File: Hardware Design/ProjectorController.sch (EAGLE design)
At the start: 12 parts, among them J1 5747844-4, J2 Cap Buttons, J3 Prog, J4 Prog/Run, U1 ESP-WROOM-32, U2 SP3232EEN-L

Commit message: USB port added and rough cut of schematic done. PC-11
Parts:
- added J5: 10118194-0001LF, 10118194-0001LF:10118194-0001LF
- R2: value (none) -> 10K
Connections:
- new net 3V3: C1.1, J3.4, J4.3, R1.1, U$1.OUT, U1.3V3, U2.VCC
- new net 5V: C2.1, J5.1, U$1.IN
- new net N$10: J1.2, U2.T1OUT
- new net N$11: J1.3, U2.R1OUT
- new net N$12: U1.IO14, U2.T1IN
- new net N$13: U1.IO12, U2.R1IN
- new net N$3: J2.3, U1.IO4
- new net N$4: R1.2, S1.2, U1.EN
- new net N$5: R2.2, U1.IO0
- new net N$6: J4.2, R2.1
- new net N$7: J3.3, U1.TXD0
- new net N$8: J3.2, U1.RXD0
- net GND: now also J1.5, J3.1, J4.1, J5.5, S1.1
- net N$1: now also J2.1, U1.IO15; no longer C1.1, U$1.OUT, U1.3V3
- net N$2: now also J2.2, U1.IO33; no longer C2.1, U$1.IN
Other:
- moved on the sheet: C1, C2, J3, J4, R1, R2, S1, U$1

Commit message: Progress on board layout PC-13
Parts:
- added C3, C4, C5, C6, C7: 0.1uF, SparkFun-Capacitors:CAP-1206
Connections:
- new net N$12: C5.2, U2.C1+
- new net N$14: C5.1, U2.C1-
- new net N$15: C4.2, U2.C2+
- new net N$16: C4.1, U2.C2-
- new net N$17: C7.2, U2.V+
- new net N$19: C6.2, U2.V-
- net 3V3: now also C3.2
- net GND: now also C3.1, C6.1, C7.1
- net N$7: now also J3.2; no longer J3.3
- net N$8: now also J3.3; no longer J3.2
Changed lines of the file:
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@@
 <part name="C2" library="SparkFun-Capacitors" deviceset="CAP" device="-1206"/>
 <part name="J5" library="10118194-0001LF" deviceset="10118194-0001LF" device=""/>
+<part name="C3" library="SparkFun-Capacitors" deviceset="CAP" device="-1206" value="0.1uF"/>
+<part name="C4" library="SparkFun-Capacitors" deviceset="CAP" device="-1206" value="0.1uF"/>
+<part name="C5" library="SparkFun-Capacitors" deviceset="CAP" device="-1206" value="0.1uF"/>
+<part name="C6" library="SparkFun-Capacitors" deviceset="CAP" device="-1206" value="0.1uF"/>
+<part name="C7" library="SparkFun-Capacitors" deviceset="CAP" device="-1206" value="0.1uF"/>
 </parts>
 <sheets>
@@
 <attribute name="NAME" x="-94.224959375" y="24.8851" size="1.271559375" layer="95" rot="R180"/>
 <attribute name="VALUE" x="-93.976059375" y="48.2639" size="1.270659375" layer="96" rot="R180"/>
+</instance>
+<instance part="C3" gate="G$1" x="40.64" y="45.72" smashed="yes">
+<attribute name="NAME" x="42.164" y="48.641" size="1.778" layer="95" font="vector"/>
+<attribute name="VALUE" x="42.164" y="43.561" size="1.778" layer="96" font="vector"/>
+</instance>
+<instance part="C4" gate="G$1" x="33.02" y="30.48" smashed="yes" rot="R180">
+<attribute name="NAME" x="31.496" y="27.559" size="1.778" layer="95" font="vector" rot="R180"/>
+<attribute name="VALUE" x="31.496" y="32.639" size="1.778" layer="96" font="vector" rot="R180"/>
+</instance>
+<instance part="C5" gate="G$1" x="38.1" y="35.56" smashed="yes" rot="R180">
+<attribute name="NAME" x="36.576" y="32.639" size="1.778" layer="95" font="vector" rot="R180"/>
+<attribute name="VALUE" x="36.576" y="37.719" size="1.778" layer="96" font="vector" rot="R180"/>
+</instance>
+<instance part="C6" gate="G$1" x="38.1" y="12.7" smashed="yes" rot="R90">
+<attribute name="NAME" x="35.179" y="14.224" size="1.778" layer="95" font="vector" rot="R90"/>
+<attribute name="VALUE" x="40.259" y="14.224" size="1.778" layer="96" font="vector" rot="R90"/>
+</instance>
+<instance part="C7" gate="G$1" x="33.02" y="40.64" smashed="yes" rot="R90">
+<attribute name="NAME" x="30.099" y="42.164" size="1.778" layer="95" font="vector" rot="R90"/>
+<attribute name="VALUE" x="35.179" y="42.164" size="1.778" layer="96" font="vector" rot="R90"/>
 </instance>
 </instances>
@@
 <wire x1="43.18" y1="7.62" x2="38.1" y2="7.62" width="0.1524" layer="91"/>
 <label x="33.02" y="7.62" size="1.778" layer="95"/>
+<pinref part="C6" gate="G$1" pin="1"/>
+<wire x1="33.02" y1="12.7" x2="33.02" y2="10.16" width="0.1524" layer="91"/>
+<wire x1="33.02" y1="10.16" x2="38.1" y2="10.16" width="0.1524" layer="91"/>
+<wire x1="38.1" y1="10.16" x2="38.1" y2="7.62" width="0.1524" layer="91"/>
 </segment>
 <segment>
@@
 <wire x1="99.06" y1="15.24" x2="93.98" y2="15.24" width="0.1524" layer="91"/>
 <label x="91.44" y="15.24" size="1.778" layer="95"/>
+</segment>
+<segment>
+<pinref part="C3" gate="G$1" pin="1"/>
+<wire x1="40.64" y1="50.8" x2="40.64" y2="53.34" width="0.1524" layer="91"/>
+<label x="40.64" y="53.34" size="1.778" layer="95"/>
+</segment>
+<segment>
+<pinref part="C7" gate="G$1" pin="1"/>
+<wire x1="27.94" y1="40.64" x2="25.4" y2="40.64" width="0.1524" layer="91"/>
+<label x="22.86" y="40.64" size="1.778" layer="95"/>
 </segment>
 </net>
@@
 <segment>
 <pinref part="U2" gate="A" pin="VCC"/>
-<wire x1="43.18" y1="43.18" x2="38.1" y2="43.18" width="0.1524" layer="91"/>
+<wire x1="43.18" y1="43.18" x2="40.64" y2="43.18" width="0.1524" layer="91"/>
 <label x="35.56" y="43.18" size="1.778" layer="95"/>
+<pinref part="C3" gate="G$1" pin="2"/>
+<wire x1="40.64" y1="43.18" x2="38.1" y2="43.18" width="0.1524" layer="91"/>
+<junction x="40.64" y="43.18"/>
 </segment>
 </net>
@@
 <pinref part="U1" gate="G$1" pin="TXD0"/>
 <wire x1="-30.48" y1="38.1" x2="-45.72" y2="38.1" width="0.1524" layer="91"/>
-<wire x1="-45.72" y1="38.1" x2="-45.72" y2="30.48" width="0.1524" layer="91"/>
-<pinref part="J3" gate="J1" pin="3"/>
-<wire x1="-45.72" y1="30.48" x2="-66.04" y2="30.48" width="0.1524" layer="91"/>
+<wire x1="-45.72" y1="38.1" x2="-45.72" y2="27.94" width="0.1524" layer="91"/>
+<pinref part="J3" gate="J1" pin="2"/>
+<wire x1="-66.04" y1="27.94" x2="-45.72" y2="27.94" width="0.1524" layer="91"/>
 </segment>
 </net>
@@
 <pinref part="U1" gate="G$1" pin="RXD0"/>
 <wire x1="-30.48" y1="35.56" x2="-43.18" y2="35.56" width="0.1524" layer="91"/>
-<wire x1="-43.18" y1="35.56" x2="-43.18" y2="27.94" width="0.1524" layer="91"/>
-<pinref part="J3" gate="J1" pin="2"/>
-<wire x1="-43.18" y1="27.94" x2="-66.04" y2="27.94" width="0.1524" layer="91"/>
+<wire x1="-43.18" y1="35.56" x2="-43.18" y2="30.48" width="0.1524" layer="91"/>
+<pinref part="J3" gate="J1" pin="3"/>
+<wire x1="-66.04" y1="30.48" x2="-43.18" y2="30.48" width="0.1524" layer="91"/>
 </segment>
 </net>
@@
 <pinref part="J1" gate="G$1" pin="3"/>
 <wire x1="88.9" y1="25.4" x2="99.06" y2="25.4" width="0.1524" layer="91"/>
-</segment>
-</net>
-<net name="N$12" class="0">
-<segment>
-<pinref part="U1" gate="G$1" pin="IO14"/>
-<wire x1="10.16" y1="43.18" x2="30.48" y2="43.18" width="0.1524" layer="91"/>
-<wire x1="30.48" y1="43.18" x2="30.48" y2="17.78" width="0.1524" layer="91"/>
-<pinref part="U2" gate="A" pin="T1IN"/>
-<wire x1="30.48" y1="17.78" x2="43.18" y2="17.78" width="0.1524" layer="91"/>
 </segment>
 </net>
@@
 </segment>
 </net>
+<net name="N$9" class="0">
+<segment>
+<pinref part="U2" gate="A" pin="T1IN"/>
+<wire x1="22.86" y1="17.78" x2="43.18" y2="17.78" width="0.1524" layer="91"/>
+<pinref part="U1" gate="G$1" pin="IO14"/>
+<wire x1="10.16" y1="43.18" x2="22.86" y2="43.18" width="0.1524" layer="91"/>
+<wire x1="22.86" y1="17.78" x2="22.86" y2="43.18" width="0.1524" layer="91"/>
+</segment>
+</net>
+<net name="N$12" class="0">
+<segment>
+<pinref part="C5" gate="G$1" pin="2"/>
+<pinref part="U2" gate="A" pin="C1+"/>
+<wire x1="38.1" y1="38.1" x2="43.18" y2="38.1" width="0.1524" layer="91"/>
+<wire x1="43.18" y1="38.1" x2="43.18" y2="35.56" width="0.1524" layer="91"/>
+</segment>
+</net>
+<net name="N$14" class="0">
+<segment>
+<pinref part="U2" gate="A" pin="C1-"/>
+<wire x1="43.18" y1="33.02" x2="40.64" y2="33.02" width="0.1524" layer="91"/>
+<wire x1="40.64" y1="33.02" x2="40.64" y2="30.48" width="0.1524" layer="91"/>
+<pinref part="C5" gate="G$1" pin="1"/>
+<wire x1="40.64" y1="30.48" x2="38.1" y2="30.48" width="0.1524" layer="91"/>
+</segment>
+</net>
+<net name="N$15" class="0">
+<segment>
+<pinref part="U2" gate="A" pin="C2+"/>
+<wire x1="43.18" y1="30.48" x2="41.656" y2="30.48" width="0.1524" layer="91"/>
+<wire x1="41.656" y1="30.48" x2="41.656" y2="28.956" width="0.1524" layer="91"/>
+<wire x1="41.656" y1="28.956" x2="41.91" y2="28.956" width="0.1524" layer="91"/>
+<wire x1="41.656" y1="28.956" x2="35.56" y2="28.956" width="0.1524" layer="91"/>
+<wire x1="35.56" y1="28.956" x2="35.56" y2="33.02" width="0.1524" layer="91"/>
+<pinref part="C4" gate="G$1" pin="2"/>
+<wire x1="35.56" y1="33.02" x2="33.02" y2="33.02" width="0.1524" layer="91"/>
+</segment>
+</net>
+<net name="N$16" class="0">
+<segment>
+<pinref part="U2" gate="A" pin="C2-"/>
+<wire x1="43.18" y1="27.94" x2="35.56" y2="27.94" width="0.1524" layer="91"/>
+<wire x1="35.56" y1="27.94" x2="35.56" y2="25.4" width="0.1524" layer="91"/>
+<pinref part="C4" gate="G$1" pin="1"/>
+<wire x1="35.56" y1="25.4" x2="33.02" y2="25.4" width="0.1524" layer="91"/>
+</segment>
+</net>
+<net name="N$17" class="0">
+<segment>
+<pinref part="U2" gate="A" pin="V+"/>
+<pinref part="C7" gate="G$1" pin="2"/>
+<wire x1="43.18" y1="40.64" x2="35.56" y2="40.64" width="0.1524" layer="91"/>
+</segment>
+</net>
+<net name="N$19" class="0">
+<segment>
+<pinref part="U2" gate="A" pin="V-"/>
+<pinref part="C6" gate="G$1" pin="2"/>
+<wire x1="43.18" y1="10.16" x2="40.64" y2="10.16" width="0.1524" layer="91"/>
+<wire x1="40.64" y1="10.16" x2="40.64" y2="12.7" width="0.1524" layer="91"/>
+</segment>
+</net>

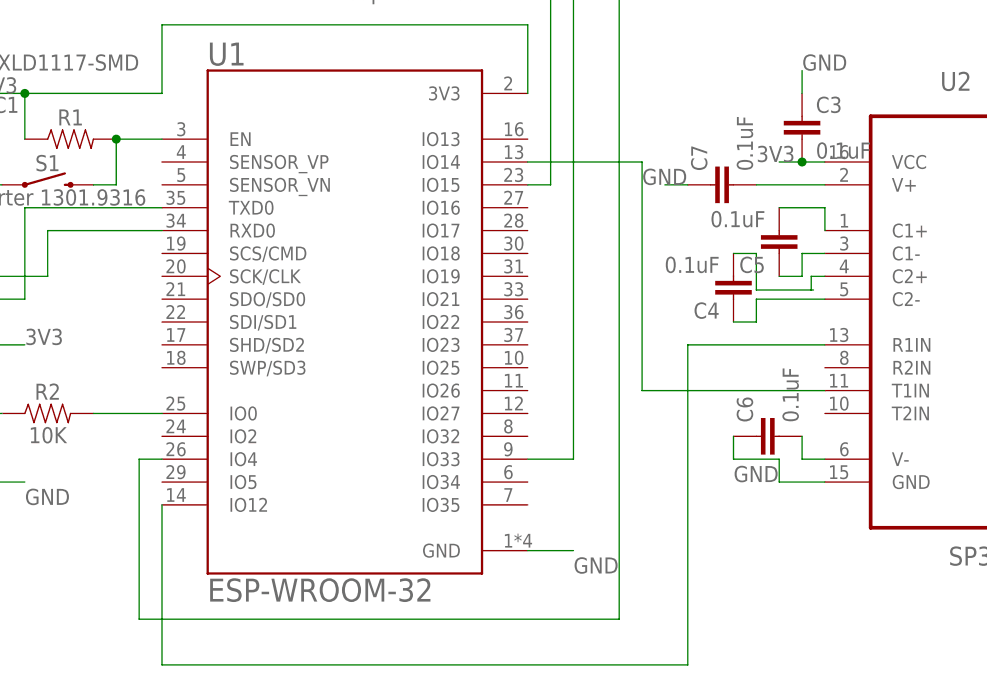
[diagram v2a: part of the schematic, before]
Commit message: Switched UART Pins PC-12
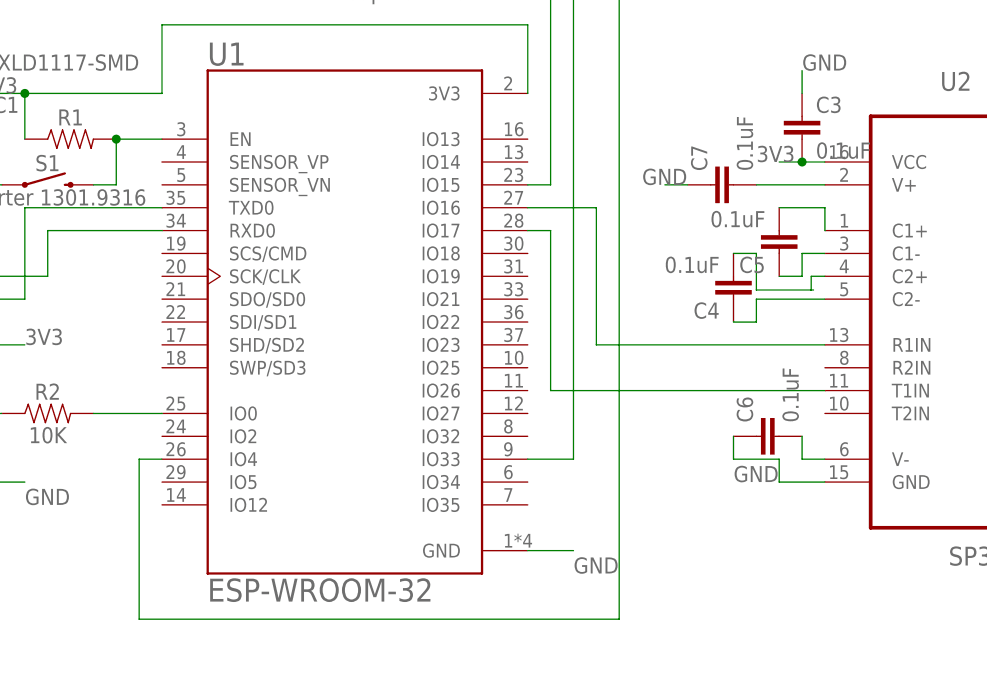
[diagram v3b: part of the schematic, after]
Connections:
- net N$13: now also U1.IO16; no longer U1.IO12
- net N$9: now also U1.IO17; no longer U1.IO14
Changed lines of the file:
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@@
 <net name="N$13" class="0">
 <segment>
-<pinref part="U1" gate="G$1" pin="IO12"/>
-<wire x1="-30.48" y1="5.08" x2="-30.48" y2="-12.7" width="0.1524" layer="91"/>
-<wire x1="-30.48" y1="-12.7" x2="27.94" y2="-12.7" width="0.1524" layer="91"/>
-<wire x1="27.94" y1="-12.7" x2="27.94" y2="22.86" width="0.1524" layer="91"/>
 <pinref part="U2" gate="A" pin="R1IN"/>
-<wire x1="27.94" y1="22.86" x2="43.18" y2="22.86" width="0.1524" layer="91"/>
+<wire x1="17.78" y1="22.86" x2="43.18" y2="22.86" width="0.1524" layer="91"/>
+<pinref part="U1" gate="G$1" pin="IO16"/>
+<wire x1="10.16" y1="38.1" x2="17.78" y2="38.1" width="0.1524" layer="91"/>
+<wire x1="17.78" y1="38.1" x2="17.78" y2="22.86" width="0.1524" layer="91"/>
 </segment>
 </net>
@@
 <segment>
 <pinref part="U2" gate="A" pin="T1IN"/>
-<wire x1="22.86" y1="17.78" x2="43.18" y2="17.78" width="0.1524" layer="91"/>
-<pinref part="U1" gate="G$1" pin="IO14"/>
-<wire x1="10.16" y1="43.18" x2="22.86" y2="43.18" width="0.1524" layer="91"/>
-<wire x1="22.86" y1="17.78" x2="22.86" y2="43.18" width="0.1524" layer="91"/>
+<wire x1="12.7" y1="17.78" x2="43.18" y2="17.78" width="0.1524" layer="91"/>
+<pinref part="U1" gate="G$1" pin="IO17"/>
+<wire x1="10.16" y1="35.56" x2="12.7" y2="35.56" width="0.1524" layer="91"/>
+<wire x1="12.7" y1="35.56" x2="12.7" y2="17.78" width="0.1524" layer="91"/>
 </segment>
 </net>

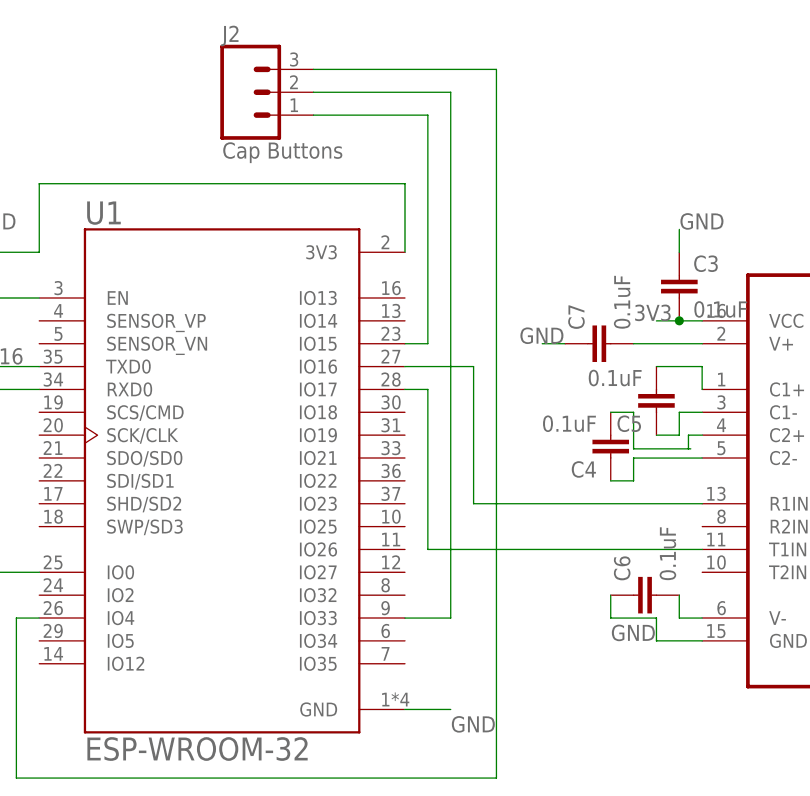
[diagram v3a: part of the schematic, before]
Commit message: Board Layout Complete PC-13
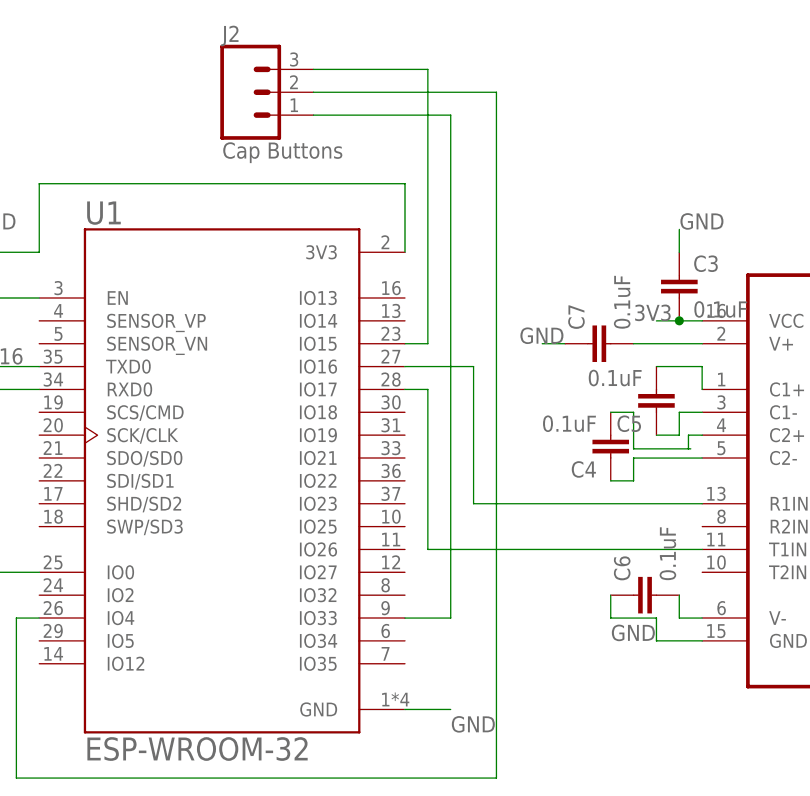
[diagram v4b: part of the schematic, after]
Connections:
- net N$1: now also J2.3; no longer J2.1
- net N$2: now also J2.1; no longer J2.2
- net N$3: now also J2.2; no longer J2.3
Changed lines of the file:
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@@
 <pinref part="U1" gate="G$1" pin="IO15"/>
 <wire x1="10.16" y1="40.64" x2="12.7" y2="40.64" width="0.1524" layer="91"/>
-<wire x1="12.7" y1="40.64" x2="12.7" y2="66.04" width="0.1524" layer="91"/>
-<pinref part="J2" gate="J$1" pin="1"/>
-<wire x1="12.7" y1="66.04" x2="0" y2="66.04" width="0.1524" layer="91"/>
+<wire x1="12.7" y1="40.64" x2="12.7" y2="71.12" width="0.1524" layer="91"/>
+<pinref part="J2" gate="J$1" pin="3"/>
+<wire x1="0" y1="71.12" x2="12.7" y2="71.12" width="0.1524" layer="91"/>
 </segment>
 </net>
@@
 <pinref part="U1" gate="G$1" pin="IO33"/>
 <wire x1="10.16" y1="10.16" x2="15.24" y2="10.16" width="0.1524" layer="91"/>
-<pinref part="J2" gate="J$1" pin="2"/>
-<wire x1="15.24" y1="10.16" x2="15.24" y2="68.58" width="0.1524" layer="91"/>
-<wire x1="15.24" y1="68.58" x2="0" y2="68.58" width="0.1524" layer="91"/>
+<wire x1="15.24" y1="10.16" x2="15.24" y2="66.04" width="0.1524" layer="91"/>
+<pinref part="J2" gate="J$1" pin="1"/>
+<wire x1="0" y1="66.04" x2="15.24" y2="66.04" width="0.1524" layer="91"/>
 </segment>
 </net>
@@
 <wire x1="-33.02" y1="10.16" x2="-33.02" y2="-7.62" width="0.1524" layer="91"/>
 <wire x1="-33.02" y1="-7.62" x2="20.32" y2="-7.62" width="0.1524" layer="91"/>
-<pinref part="J2" gate="J$1" pin="3"/>
-<wire x1="20.32" y1="-7.62" x2="20.32" y2="71.12" width="0.1524" layer="91"/>
-<wire x1="20.32" y1="71.12" x2="0" y2="71.12" width="0.1524" layer="91"/>
+<wire x1="20.32" y1="-7.62" x2="20.32" y2="68.58" width="0.1524" layer="91"/>
+<pinref part="J2" gate="J$1" pin="2"/>
+<wire x1="0" y1="68.58" x2="20.32" y2="68.58" width="0.1524" layer="91"/>
 </segment>
 </net>

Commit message: Optimised Layout
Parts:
- C1, C2: value (none) -> 10uF
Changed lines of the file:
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@@
 <part name="J4" library="SparkFun-Connectors" deviceset="CONN_03" device="" value="Prog/Run"/>
 <part name="U$1" library="SparkFun-IC-Power" deviceset="V_REG_LD1117VXX" device="LD1117-SMD"/>
-<part name="C1" library="SparkFun-Capacitors" deviceset="CAP" device="-1206"/>
-<part name="C2" library="SparkFun-Capacitors" deviceset="CAP" device="-1206"/>
+<part name="C1" library="SparkFun-Capacitors" deviceset="CAP" device="-1206" value="10uF"/>
+<part name="C2" library="SparkFun-Capacitors" deviceset="CAP" device="-1206" value="10uF"/>
 <part name="J5" library="10118194-0001LF" deviceset="10118194-0001LF" device=""/>
 <part name="C3" library="SparkFun-Capacitors" deviceset="CAP" device="-1206" value="0.1uF"/>
@@
 <label x="35.56" y="43.18" size="1.778" layer="95"/>
 <pinref part="C3" gate="G$1" pin="2"/>
-<wire x1="40.64" y1="43.18" x2="38.1" y2="43.18" width="0.1524" layer="91"/>
-<junction x="40.64" y="43.18"/>
 </segment>
 </net>
@@
 <wire x1="43.18" y1="30.48" x2="41.656" y2="30.48" width="0.1524" layer="91"/>
 <wire x1="41.656" y1="30.48" x2="41.656" y2="28.956" width="0.1524" layer="91"/>
-<wire x1="41.656" y1="28.956" x2="41.91" y2="28.956" width="0.1524" layer="91"/>
 <wire x1="41.656" y1="28.956" x2="35.56" y2="28.956" width="0.1524" layer="91"/>
 <wire x1="35.56" y1="28.956" x2="35.56" y2="33.02" width="0.1524" layer="91"/>

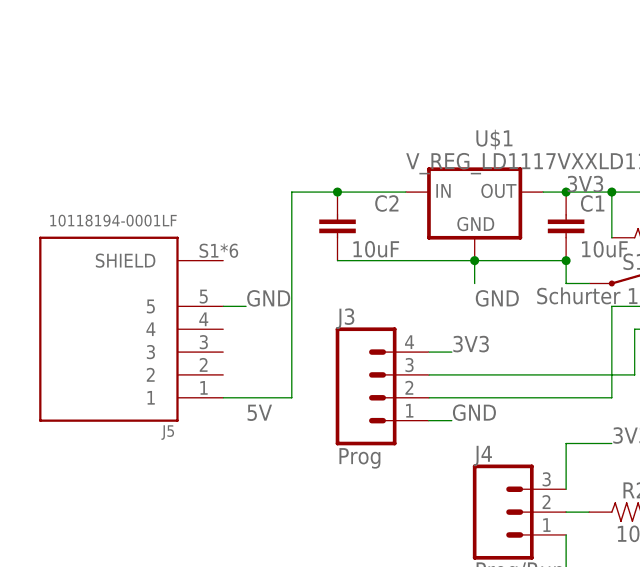
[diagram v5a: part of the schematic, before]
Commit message: Revert "Revert "ED-33 Major board redesign to make smaller""
This reverts commit 3ae201e74c16ce24ee355c7bdbcad0014f833ec8.
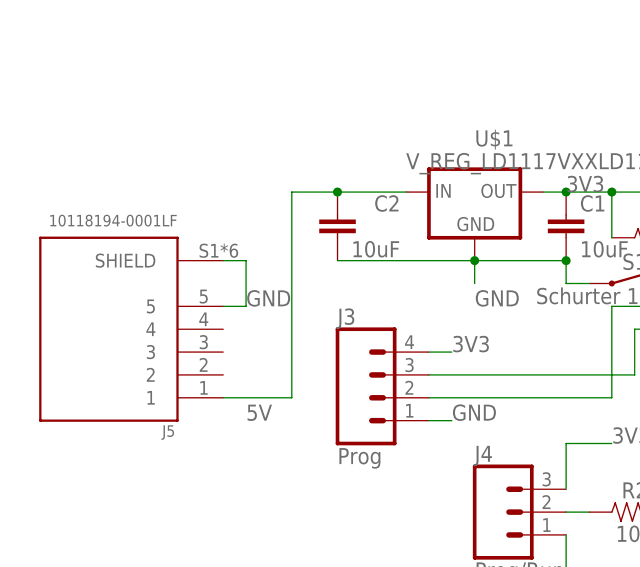
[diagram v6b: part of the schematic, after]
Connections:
- net GND: now also J5.SHIELD
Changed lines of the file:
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@@
 <?xml version="1.0" encoding="utf-8"?>
 <!DOCTYPE eagle SYSTEM "eagle.dtd">
-<eagle version="9.5.2">
+<eagle version="9.6.1">
 <drawing>
 <settings>
@@
 <wire x1="-88.9" y1="38.1" x2="-86.36" y2="38.1" width="0.1524" layer="91"/>
 <label x="-86.36" y="38.1" size="1.778" layer="95"/>
-</segment>
-<segment>
+<pinref part="J5" gate="G$1" pin="SHIELD"/>
+<wire x1="-88.9" y1="43.18" x2="-86.36" y2="43.18" width="0.1524" layer="91"/>
+<wire x1="-86.36" y1="43.18" x2="-86.36" y2="38.1" width="0.1524" layer="91"/>
+</segment>
+<segment>
